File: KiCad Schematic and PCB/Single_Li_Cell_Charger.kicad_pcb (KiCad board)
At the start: 2 copper layers, 33.5 x 20.3 mm, 13 parts, among them J1 USB_B_Micro, J2 VDD, J3 STAT, J4 PROG, J5 +BATT, J6 GND, U1 MCP73832T-2DCI/OT

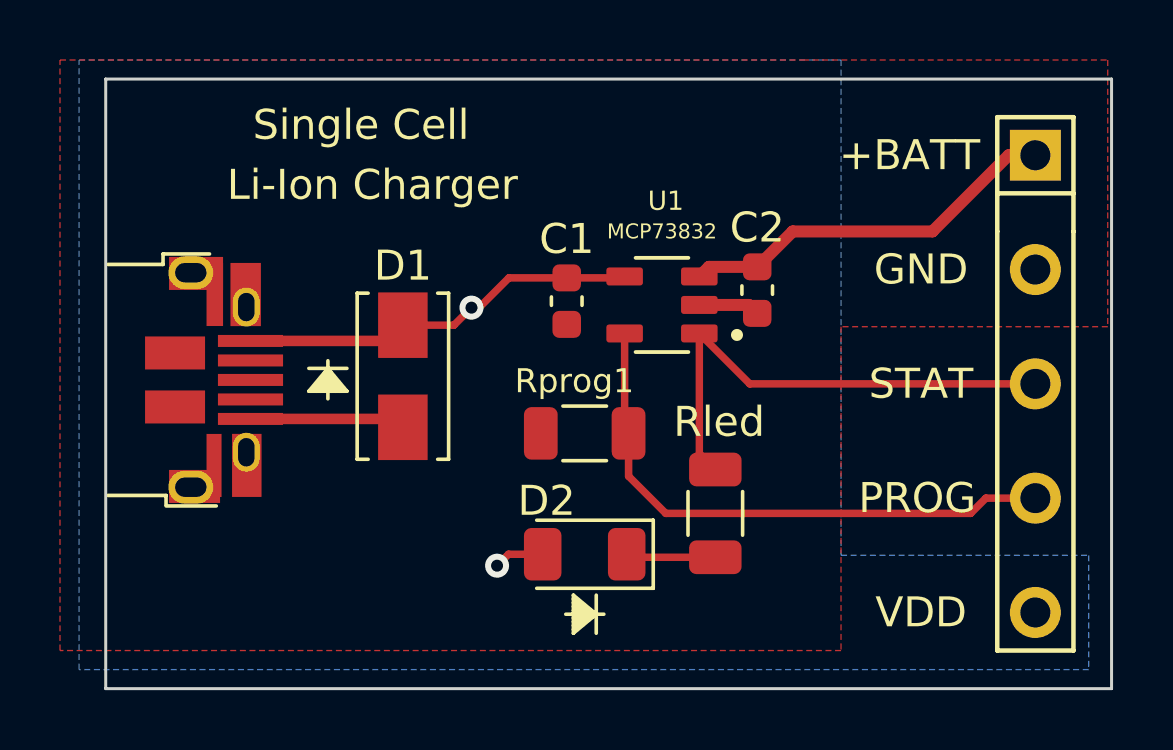
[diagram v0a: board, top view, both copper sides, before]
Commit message: V2
V2- Updated MicroUSB footprint and changed header pins so it will fit a row of pin headers instead of them being spaced out.
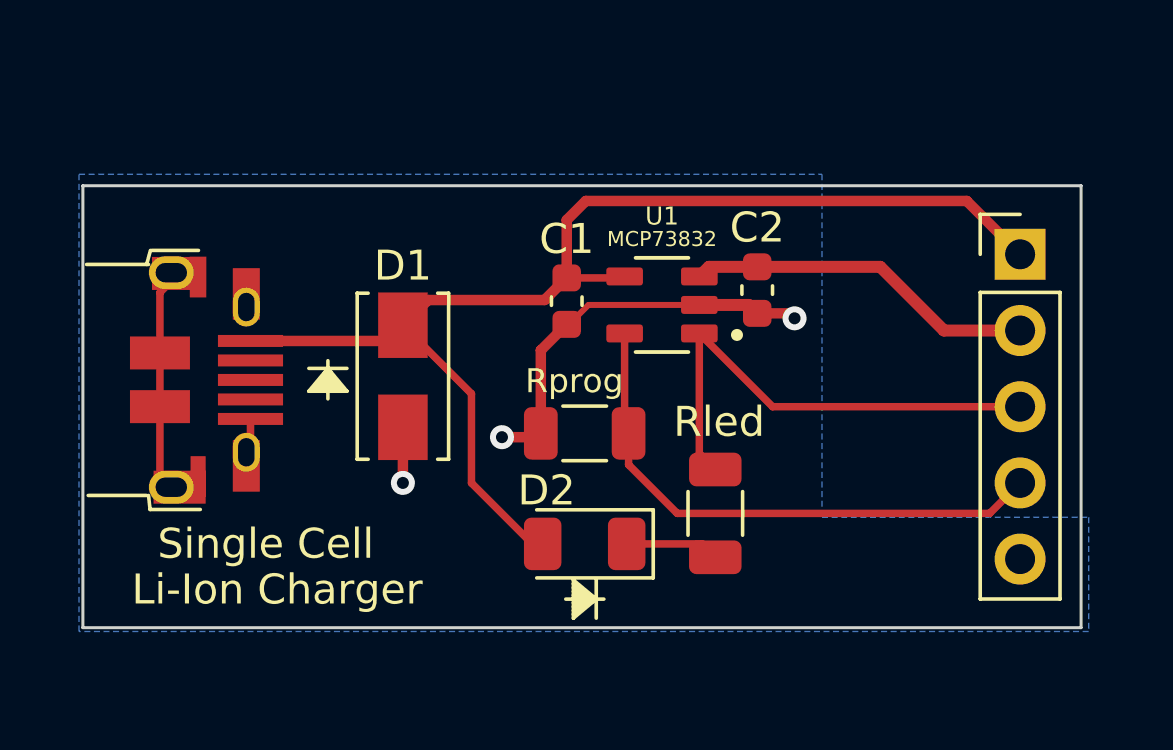
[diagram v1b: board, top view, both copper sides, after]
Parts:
- removed J2: VDD, Connector_PinSocket_2.54mm:PinSocket_1x01_P2.54mm_Vertical
- removed J3: STAT, Connector_PinSocket_2.54mm:PinSocket_1x01_P2.54mm_Vertical
- removed J5: +BATT, Connector_PinSocket_2.54mm:PinSocket_1x01_P2.54mm_Vertical
- removed J6: GND, Connector_PinSocket_2.54mm:PinSocket_1x01_P2.54mm_Vertical
- J1: footprint allied_connectors_usb:micro_usb_b_2.0_horizontal -> AMUSB464:micro_usb_b_2.0_horizontal
- J4: value PROG -> Conn_01x05; footprint Connector_PinSocket_2.54mm:PinSocket_1x01_P2.54mm_Vertical -> Connector_PinHeader_2.54mm:PinHeader_1x05_P2.54mm_Vertical
- moved J4 8.14 mm to (48.5, 19.8)
- moved D2 0.35 mm to (34.0, 29.5)
- renumbered Rprog1 to Rprog
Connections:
- C1 pad 1: VDD -> VBUS
- D1 pad 1: VDD -> VBUS
- D2 pad 2: VDD -> VBUS
- J1 pad 1: VDD -> VBUS
- J4 pad 1: Net-(J4-Pad1) -> VBUS
- Rled pad 2: Net-(J3-Pad1) -> /STAT
- Rprog pad 1: Net-(J4-Pad1) -> /PROG
- U1 pad 1: Net-(J3-Pad1) -> /STAT
- U1 pad 4: VDD -> VBUS
- U1 pad 5: Net-(J4-Pad1) -> /PROG
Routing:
- net VBUS: track 0.00 -> 40.8 mm
- net Net-(J4-Pad1): track 19.1 -> 0.00 mm
- net /PROG: track 0.00 -> 18.6 mm
- net -BATT: track 7.24 -> 24.0 mm, vias 0 -> 3
- net Net-(J3-Pad1): track 16.7 -> 0.00 mm
- net /STAT: track 0.00 -> 16.5 mm
- net VDD: track 15.0 -> 0.00 mm, vias 2 -> 0
- net +BATT: track 12.9 -> 11.7 mm
- added copper zone on B.Cu, net -BATT
- removed copper zone on F.Cu, net -BATT
- removed copper zone on B.Cu, net VDD
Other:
- board size 33.5 x 20.3 mm -> 33.3 x 14.7 mm

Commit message: Edge Cuts Fixed
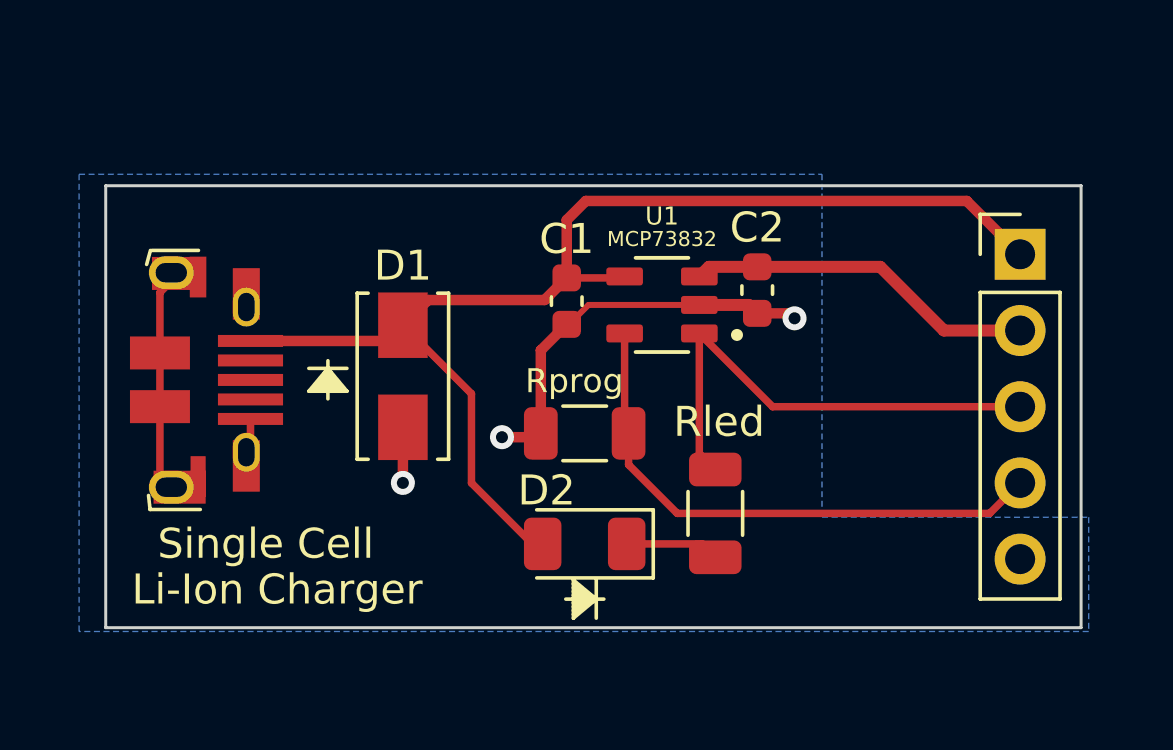
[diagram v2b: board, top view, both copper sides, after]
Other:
- board size 33.3 x 14.7 mm -> 32.5 x 14.7 mm
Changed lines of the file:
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@@
       (effects (font (size 1 1) (thickness 0.15)))
-    )
-    (fp_text user "pcb edge" (at 0 0.381 -90 unlocked) (layer "F.Fab")
-      (effects (font (size 0.5 0.5) (thickness 0.1)))
     )
     (fp_line (start 4.318 -1.0675) (end 4.318 -2.7425) (layer "F.SilkS") (width 0.12))
@@
     (fp_line (start -4.318 -1.0795) (end -3.85 -0.9525) (layer "F.SilkS") (width 0.12))
     (fp_line (start -4.318 -1.13) (end -4.318 -2.68) (layer "F.SilkS") (width 0.12))
-    (fp_line (start -3.85 1.0495) (end -3.85 -1.016) (layer "F.SilkS") (width 0.12))
-    (fp_line (start 3.85 0.995) (end 3.85 -0.95) (layer "F.SilkS") (width 0.12))
     (fp_line (start -4.3 -5.6) (end 4.4 -5.6) (layer "F.CrtYd") (width 0.05))
     (fp_line (start 4.4 1.19) (end 4.4 -5.6) (layer "F.CrtYd") (width 0.05))
@@
     (fp_line (start -4.3 -5.6) (end -4.3 1.19) (layer "F.CrtYd") (width 0.05))
     (fp_line (start -3.75 -3.255) (end -2.95 -4.005) (layer "F.Fab") (width 0.1))
-    (fp_line (start -3.75 0.945) (end -3.75 -3.255) (layer "F.Fab") (width 0.12))
-    (fp_line (start 3.75 0.945) (end -3.75 0.945) (layer "F.Fab") (width 0.12))
-    (fp_line (start -3.85 0.945) (end 3.85 0.945) (layer "F.Fab") (width 0.1))
+    (fp_line (start -3.85 0) (end 3.85 0) (layer "F.Fab") (width 0.1))
     (fp_line (start -2.95 -4.005) (end 3.75 -4.005) (layer "F.Fab") (width 0.12))
-    (fp_line (start 3.75 -4.005) (end 3.75 0.945) (layer "F.Fab") (width 0.12))
     (pad "1" smd rect (at -1.3 -4.415) (size 2.17 0.4) (layers "F.Cu" "F.Paste" "F.Mask")
       (net 9 "VBUS") (pinfunction "VBUS") (pintype "power_out"))
@@
       (effects (font (size 1 1) (thickness 0.15)))
     )
-    (fp_text value "Conn_01x05" (at 0 12.49) (layer "F.Fab")
+    (fp_text value "Conn_01x05" (at 0 12.49) (layer "F.Fab") hide
       (effects (font (size 1 1) (thickness 0.15)))
     )
@@
     )
   )
-  (gr_line (start 17.272 32.258) (end 50.546 32.258) (layer "Edge.Cuts") (width 0.1))
-  (gr_line (start 17.272 32.258) (end 17.272 17.526) (layer "Edge.Cuts") (width 0.1))
-  (gr_line (start 50.546 17.526) (end 17.272 17.526) (layer "Edge.Cuts") (width 0.1))
+  (gr_line (start 18.034 32.258) (end 50.546 32.258) (layer "Edge.Cuts") (width 0.1))
+  (gr_line (start 18.034 32.258) (end 18.034 17.526) (layer "Edge.Cuts") (width 0.1))
+  (gr_line (start 50.546 17.526) (end 18.034 17.526) (layer "Edge.Cuts") (width 0.1))
   (gr_line (start 50.546 17.526) (end 50.546 32.258) (layer "Edge.Cuts") (width 0.1))
   (gr_text "Li-Ion Charger" (at 23.749 30.988) (layer "F.SilkS")
